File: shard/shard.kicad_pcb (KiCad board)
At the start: 2 copper layers, 35 x 25 mm, 2 parts, among them J0 Shard

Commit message: shard template fixed
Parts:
- J0: moved to F.Cu
- moved J0 2.50 mm to (125.0, 57.5), turned to 90 degrees
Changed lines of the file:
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@@
     )
   )
-  (module Connector_PinHeader_2.54mm:PinHeader_2x10_P2.54mm_Vertical (layer B.Cu)
-    (at 125 55 270)
+  (module Connector_PinHeader_2.54mm:PinHeader_2x10_P2.54mm_Vertical (layer F.Cu)
+    (at 125 57.5 90)
     (descr "Through hole straight pin header, 2x10, 2.54mm pitch, double rows")
     (tags "Through hole pin header THT 2x10 2.54mm double row")
-    (fp_text reference J0 (at 1.27 2.33 270) (layer B.Fab)
-      (effects (font (size 1 1) (thickness 0.15)) (justify mirror))
+    (fp_text reference J0 (at 1.27 -2.33 90) (layer F.Fab)
+      (effects (font (size 1 1) (thickness 0.15)))
     )
-    (fp_text value Shard (at 1.27 -25.19 270) (layer B.SilkS)
-      (effects (font (size 1 1) (thickness 0.15)) (justify mirror))
+    (fp_text value Shard (at 1.27 25.19 90) (layer F.SilkS)
+      (effects (font (size 1 1) (thickness 0.15)))
     )
-    (fp_line (start 0 1.27) (end 3.81 1.27) (layer B.Fab) (width 0.1))
-    (fp_line (start 3.81 1.27) (end 3.81 -24.13) (layer B.Fab) (width 0.1))
-    (fp_line (start 3.81 -24.13) (end -1.27 -24.13) (layer B.Fab) (width 0.1))
-    (fp_line (start -1.27 -24.13) (end -1.27 0) (layer B.Fab) (width 0.1))
-    (fp_line (start -1.27 0) (end 0 1.27) (layer B.Fab) (width 0.1))
-    (fp_line (start -1.33 -24.19) (end 3.87 -24.19) (layer B.SilkS) (width 0.12))
-    (fp_line (start -1.33 -1.27) (end -1.33 -24.19) (layer B.SilkS) (width 0.12))
-    (fp_line (start 3.87 1.33) (end 3.87 -24.19) (layer B.SilkS) (width 0.12))
-    (fp_line (start -1.33 -1.27) (end 1.27 -1.27) (layer B.SilkS) (width 0.12))
-    (fp_line (start 1.27 -1.27) (end 1.27 1.33) (layer B.SilkS) (width 0.12))
-    (fp_line (start 1.27 1.33) (end 3.87 1.33) (layer B.SilkS) (width 0.12))
-    (fp_line (start -1.33 0) (end -1.33 1.33) (layer B.SilkS) (width 0.12))
-    (fp_line (start -1.33 1.33) (end 0 1.33) (layer B.SilkS) (width 0.12))
-    (fp_line (start -1.8 1.8) (end -1.8 -24.65) (layer B.CrtYd) (width 0.05))
-    (fp_line (start -1.8 -24.65) (end 4.35 -24.65) (layer B.CrtYd) (width 0.05))
-    (fp_line (start 4.35 -24.65) (end 4.35 1.8) (layer B.CrtYd) (width 0.05))
-    (fp_line (start 4.35 1.8) (end -1.8 1.8) (layer B.CrtYd) (width 0.05))
-    (fp_text user %R (at 1.27 -11.43 180) (layer B.Fab)
-      (effects (font (size 1 1) (thickness 0.15)) (justify mirror))
+    (fp_line (start 0 -1.27) (end 3.81 -1.27) (layer F.Fab) (width 0.1))
+    (fp_line (start 3.81 -1.27) (end 3.81 24.13) (layer F.Fab) (width 0.1))
+    (fp_line (start 3.81 24.13) (end -1.27 24.13) (layer F.Fab) (width 0.1))
+    (fp_line (start -1.27 24.13) (end -1.27 0) (layer F.Fab) (width 0.1))
+    (fp_line (start -1.27 0) (end 0 -1.27) (layer F.Fab) (width 0.1))
+    (fp_line (start -1.33 24.19) (end 3.87 24.19) (layer F.SilkS) (width 0.12))
+    (fp_line (start -1.33 1.27) (end -1.33 24.19) (layer F.SilkS) (width 0.12))
+    (fp_line (start 3.87 -1.33) (end 3.87 24.19) (layer F.SilkS) (width 0.12))
+    (fp_line (start -1.33 1.27) (end 1.27 1.27) (layer F.SilkS) (width 0.12))
+    (fp_line (start 1.27 1.27) (end 1.27 -1.33) (layer F.SilkS) (width 0.12))
+    (fp_line (start 1.27 -1.33) (end 3.87 -1.33) (layer F.SilkS) (width 0.12))
+    (fp_line (start -1.33 0) (end -1.33 -1.33) (layer F.SilkS) (width 0.12))
+    (fp_line (start -1.33 -1.33) (end 0 -1.33) (layer F.SilkS) (width 0.12))
+    (fp_line (start -1.8 -1.8) (end -1.8 24.65) (layer F.CrtYd) (width 0.05))
+    (fp_line (start -1.8 24.65) (end 4.35 24.65) (layer F.CrtYd) (width 0.05))
+    (fp_line (start 4.35 24.65) (end 4.35 -1.8) (layer F.CrtYd) (width 0.05))
+    (fp_line (start 4.35 -1.8) (end -1.8 -1.8) (layer F.CrtYd) (width 0.05))
+    (fp_text user %R (at 1.27 11.43 180) (layer F.Fab)
+      (effects (font (size 1 1) (thickness 0.15)))
     )
-    (pad 1 thru_hole rect (at 0 0 270) (size 1.7 1.7) (drill 1) (layers *.Cu *.Mask)
+    (pad 1 thru_hole rect (at 0 0 90) (size 1.7 1.7) (drill 1) (layers *.Cu *.Mask)
       (net 1 +3V3))
-    (pad 2 thru_hole oval (at 2.54 0 270) (size 1.7 1.7) (drill 1) (layers *.Cu *.Mask)
+    (pad 2 thru_hole oval (at 2.54 0 90) (size 1.7 1.7) (drill 1) (layers *.Cu *.Mask)
       (net 3 D_CS))
-    (pad 3 thru_hole oval (at 0 -2.54 270) (size 1.7 1.7) (drill 1) (layers *.Cu *.Mask)
+    (pad 3 thru_hole oval (at 0 2.54 90) (size 1.7 1.7) (drill 1) (layers *.Cu *.Mask)
       (net 4 UP))
-    (pad 4 thru_hole oval (at 2.54 -2.54 270) (size 1.7 1.7) (drill 1) (layers *.Cu *.Mask)
+    (pad 4 thru_hole oval (at 2.54 2.54 90) (size 1.7 1.7) (drill 1) (layers *.Cu *.Mask)
       (net 5 D_DC))
-    (pad 5 thru_hole oval (at 0 -5.08 270) (size 1.7 1.7) (drill 1) (layers *.Cu *.Mask)
+    (pad 5 thru_hole oval (at 0 5.08 90) (size 1.7 1.7) (drill 1) (layers *.Cu *.Mask)
       (net 6 DOWN))
-    (pad 6 thru_hole oval (at 2.54 -5.08 270) (size 1.7 1.7) (drill 1) (layers *.Cu *.Mask)
+    (pad 6 thru_hole oval (at 2.54 5.08 90) (size 1.7 1.7) (drill 1) (layers *.Cu *.Mask)
       (net 7 D_RST))
-    (pad 7 thru_hole oval (at 0 -7.62 270) (size 1.7 1.7) (drill 1) (layers *.Cu *.Mask)
+    (pad 7 thru_hole oval (at 0 7.62 90) (size 1.7 1.7) (drill 1) (layers *.Cu *.Mask)
       (net 8 LEFT))
-    (pad 8 thru_hole oval (at 2.54 -7.62 270) (size 1.7 1.7) (drill 1) (layers *.Cu *.Mask)
+    (pad 8 thru_hole oval (at 2.54 7.62 90) (size 1.7 1.7) (drill 1) (layers *.Cu *.Mask)
       (net 9 D_MOSI))
-    (pad 9 thru_hole oval (at 0 -10.16 270) (size 1.7 1.7) (drill 1) (layers *.Cu *.Mask)
+    (pad 9 thru_hole oval (at 0 10.16 90) (size 1.7 1.7) (drill 1) (layers *.Cu *.Mask)
       (net 10 RIGHT))
-    (pad 10 thru_hole oval (at 2.54 -10.16 270) (size 1.7 1.7) (drill 1) (layers *.Cu *.Mask)
+    (pad 10 thru_hole oval (at 2.54 10.16 90) (size 1.7 1.7) (drill 1) (layers *.Cu *.Mask)
       (net 11 D_SCK))
-    (pad 11 thru_hole oval (at 0 -12.7 270) (size 1.7 1.7) (drill 1) (layers *.Cu *.Mask)
+    (pad 11 thru_hole oval (at 0 12.7 90) (size 1.7 1.7) (drill 1) (layers *.Cu *.Mask)
       (net 12 SND))
-    (pad 12 thru_hole oval (at 2.54 -12.7 270) (size 1.7 1.7) (drill 1) (layers *.Cu *.Mask)
+    (pad 12 thru_hole oval (at 2.54 12.7 90) (size 1.7 1.7) (drill 1) (layers *.Cu *.Mask)
       (net 2 D+))
-    (pad 13 thru_hole oval (at 0 -15.24 270) (size 1.7 1.7) (drill 1) (layers *.Cu *.Mask)
+    (pad 13 thru_hole oval (at 0 15.24 90) (size 1.7 1.7) (drill 1) (layers *.Cu *.Mask)
       (net 13 RESET))
-    (pad 14 thru_hole oval (at 2.54 -15.24 270) (size 1.7 1.7) (drill 1) (layers *.Cu *.Mask)
+    (pad 14 thru_hole oval (at 2.54 15.24 90) (size 1.7 1.7) (drill 1) (layers *.Cu *.Mask)
       (net 2 D+))
-    (pad 15 thru_hole oval (at 0 -17.78 270) (size 1.7 1.7) (drill 1) (layers *.Cu *.Mask)
+    (pad 15 thru_hole oval (at 0 17.78 90) (size 1.7 1.7) (drill 1) (layers *.Cu *.Mask)
       (net 14 BTN_C))
-    (pad 16 thru_hole oval (at 2.54 -17.78 270) (size 1.7 1.7) (drill 1) (layers *.Cu *.Mask)
+    (pad 16 thru_hole oval (at 2.54 17.78 90) (size 1.7 1.7) (drill 1) (layers *.Cu *.Mask)
       (net 2 D+))
-    (pad 17 thru_hole oval (at 0 -20.32 270) (size 1.7 1.7) (drill 1) (layers *.Cu *.Mask)
+    (pad 17 thru_hole oval (at 0 20.32 90) (size 1.7 1.7) (drill 1) (layers *.Cu *.Mask)
       (net 15 BTN_B))
-    (pad 18 thru_hole oval (at 2.54 -20.32 270) (size 1.7 1.7) (drill 1) (layers *.Cu *.Mask)
+    (pad 18 thru_hole oval (at 2.54 20.32 90) (size 1.7 1.7) (drill 1) (layers *.Cu *.Mask)
       (net 2 D+))
-    (pad 19 thru_hole oval (at 0 -22.86 270) (size 1.7 1.7) (drill 1) (layers *.Cu *.Mask)
+    (pad 19 thru_hole oval (at 0 22.86 90) (size 1.7 1.7) (drill 1) (layers *.Cu *.Mask)
       (net 16 BTN_A))
-    (pad 20 thru_hole oval (at 2.54 -22.86 270) (size 1.7 1.7) (drill 1) (layers *.Cu *.Mask)
+    (pad 20 thru_hole oval (at 2.54 22.86 90) (size 1.7 1.7) (drill 1) (layers *.Cu *.Mask)
       (net 2 D+))
     (model ${KISYS3DMOD}/Connector_PinHeader_2.54mm.3dshapes/PinHeader_2x10_P2.54mm_Vertical.wrl

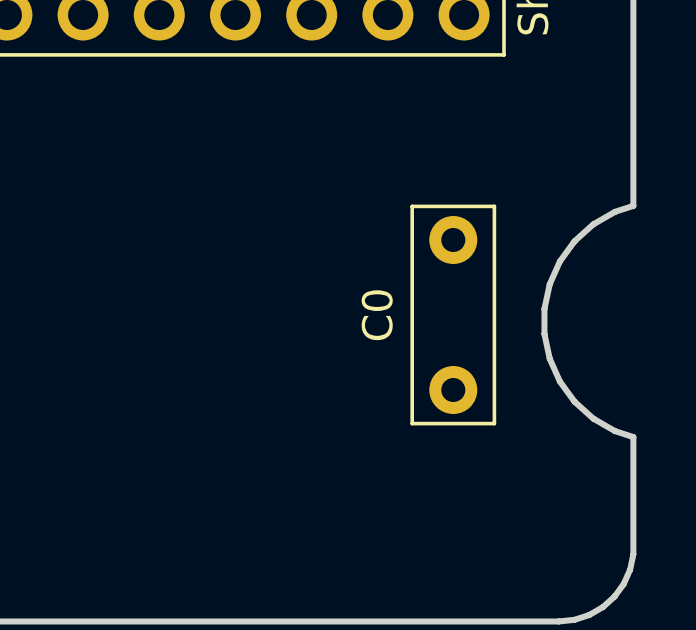
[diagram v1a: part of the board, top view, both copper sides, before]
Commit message: added capacitor value
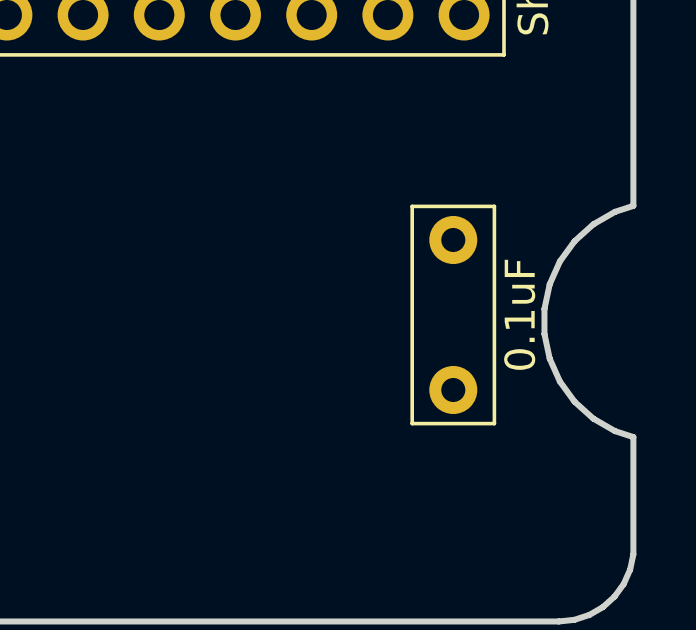
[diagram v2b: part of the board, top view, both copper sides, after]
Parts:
- C0: value C -> 0.1uF
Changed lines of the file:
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@@
     (descr "C, Rect series, Radial, pin pitch=5.00mm, , length*width=7*2.5mm^2, Capacitor")
     (tags "C Rect series Radial pin pitch 5.00mm  length 7mm width 2.5mm Capacitor")
-    (fp_text reference C0 (at 2.5 -2.5 90) (layer F.SilkS)
+    (fp_text reference C0 (at 2.5 0 90) (layer F.Fab)
       (effects (font (size 1 1) (thickness 0.15)))
     )
-    (fp_text value C (at 2.5 2.5 90) (layer F.Fab)
+    (fp_text value 0.1uF (at 2.5 2.25 90) (layer F.SilkS)
       (effects (font (size 1 1) (thickness 0.15)))
     )

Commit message: disconnected D- & D+ to fix GND net
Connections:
- net D+ renamed GND
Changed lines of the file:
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@@
   (net 0 "")
   (net 1 +3V3)
-  (net 2 D+)
-  (net 3 D_CS)
-  (net 4 UP)
-  (net 5 D_DC)
-  (net 6 DOWN)
-  (net 7 D_RST)
-  (net 8 LEFT)
-  (net 9 D_MOSI)
-  (net 10 RIGHT)
-  (net 11 D_SCK)
-  (net 12 SND)
-  (net 13 RESET)
-  (net 14 BTN_C)
-  (net 15 BTN_B)
-  (net 16 BTN_A)
+  (net 2 D_CS)
+  (net 3 UP)
+  (net 4 D_DC)
+  (net 5 DOWN)
+  (net 6 D_RST)
+  (net 7 LEFT)
+  (net 8 D_MOSI)
+  (net 9 RIGHT)
+  (net 10 D_SCK)
+  (net 11 SND)
+  (net 12 RESET)
+  (net 13 BTN_C)
+  (net 14 BTN_B)
+  (net 15 BTN_A)
+  (net 16 GND)
   (net_class Default "This is the default net class."
     (clearance 0.2)
@@
     (add_net BTN_B)
     (add_net BTN_C)
-    (add_net D+)
     (add_net DOWN)
     (add_net D_CS)
@@
     (add_net D_RST)
     (add_net D_SCK)
+    (add_net GND)
     (add_net LEFT)
     (add_net RESET)
@@
       (net 1 +3V3))
     (pad 2 thru_hole circle (at 5 0 90) (size 1.6 1.6) (drill 0.8) (layers *.Cu *.Mask)
-      (net 2 D+))
+      (net 16 GND))
     (model ${KISYS3DMOD}/Capacitor_THT.3dshapes/C_Rect_L7.0mm_W2.5mm_P5.00mm.wrl
       (at (xyz 0 0 0))
@@
       (net 1 +3V3))
     (pad 2 thru_hole oval (at 2.54 0 90) (size 1.7 1.7) (drill 1) (layers *.Cu *.Mask)
-      (net 3 D_CS))
+      (net 2 D_CS))
     (pad 3 thru_hole oval (at 0 2.54 90) (size 1.7 1.7) (drill 1) (layers *.Cu *.Mask)
-      (net 4 UP))
+      (net 3 UP))
     (pad 4 thru_hole oval (at 2.54 2.54 90) (size 1.7 1.7) (drill 1) (layers *.Cu *.Mask)
-      (net 5 D_DC))
+      (net 4 D_DC))
     (pad 5 thru_hole oval (at 0 5.08 90) (size 1.7 1.7) (drill 1) (layers *.Cu *.Mask)
-      (net 6 DOWN))
+      (net 5 DOWN))
     (pad 6 thru_hole oval (at 2.54 5.08 90) (size 1.7 1.7) (drill 1) (layers *.Cu *.Mask)
-      (net 7 D_RST))
+      (net 6 D_RST))
     (pad 7 thru_hole oval (at 0 7.62 90) (size 1.7 1.7) (drill 1) (layers *.Cu *.Mask)
-      (net 8 LEFT))
+      (net 7 LEFT))
     (pad 8 thru_hole oval (at 2.54 7.62 90) (size 1.7 1.7) (drill 1) (layers *.Cu *.Mask)
-      (net 9 D_MOSI))
+      (net 8 D_MOSI))
     (pad 9 thru_hole oval (at 0 10.16 90) (size 1.7 1.7) (drill 1) (layers *.Cu *.Mask)
-      (net 10 RIGHT))
+      (net 9 RIGHT))
     (pad 10 thru_hole oval (at 2.54 10.16 90) (size 1.7 1.7) (drill 1) (layers *.Cu *.Mask)
-      (net 11 D_SCK))
+      (net 10 D_SCK))
     (pad 11 thru_hole oval (at 0 12.7 90) (size 1.7 1.7) (drill 1) (layers *.Cu *.Mask)
-      (net 12 SND))
+      (net 11 SND))
     (pad 12 thru_hole oval (at 2.54 12.7 90) (size 1.7 1.7) (drill 1) (layers *.Cu *.Mask)
-      (net 2 D+))
+      (net 16 GND))
     (pad 13 thru_hole oval (at 0 15.24 90) (size 1.7 1.7) (drill 1) (layers *.Cu *.Mask)
-      (net 13 RESET))
+      (net 12 RESET))
     (pad 14 thru_hole oval (at 2.54 15.24 90) (size 1.7 1.7) (drill 1) (layers *.Cu *.Mask)
-      (net 2 D+))
+      (net 16 GND))
     (pad 15 thru_hole oval (at 0 17.78 90) (size 1.7 1.7) (drill 1) (layers *.Cu *.Mask)
-      (net 14 BTN_C))
+      (net 13 BTN_C))
     (pad 16 thru_hole oval (at 2.54 17.78 90) (size 1.7 1.7) (drill 1) (layers *.Cu *.Mask)
-      (net 2 D+))
+      (net 16 GND))
     (pad 17 thru_hole oval (at 0 20.32 90) (size 1.7 1.7) (drill 1) (layers *.Cu *.Mask)
-      (net 15 BTN_B))
+      (net 14 BTN_B))
     (pad 18 thru_hole oval (at 2.54 20.32 90) (size 1.7 1.7) (drill 1) (layers *.Cu *.Mask)
-      (net 2 D+))
+      (net 16 GND))
     (pad 19 thru_hole oval (at 0 22.86 90) (size 1.7 1.7) (drill 1) (layers *.Cu *.Mask)
-      (net 16 BTN_A))
+      (net 15 BTN_A))
     (pad 20 thru_hole oval (at 2.54 22.86 90) (size 1.7 1.7) (drill 1) (layers *.Cu *.Mask)
-      (net 2 D+))
+      (net 16 GND))
     (model ${KISYS3DMOD}/Connector_PinHeader_2.54mm.3dshapes/PinHeader_2x10_P2.54mm_Vertical.wrl
       (at (xyz 0 0 0))

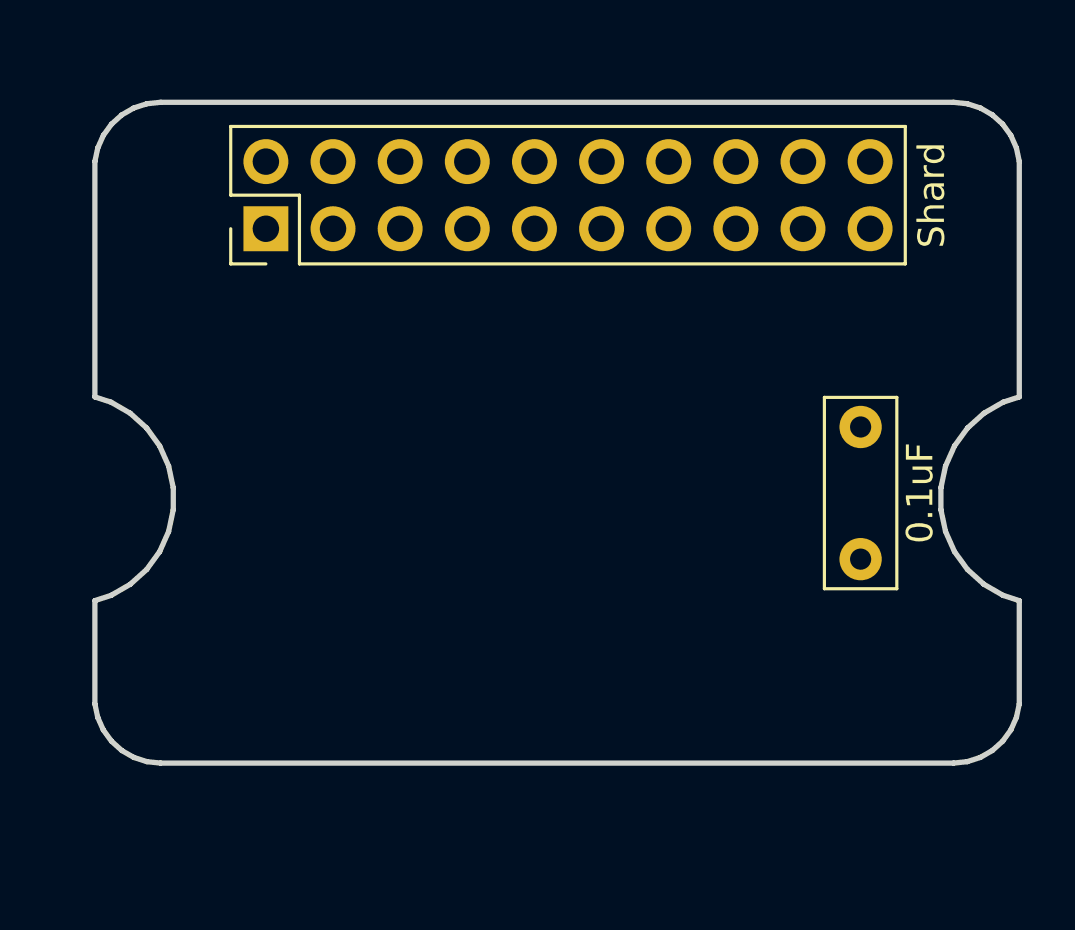
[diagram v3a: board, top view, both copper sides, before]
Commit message: Template updated to edge connector
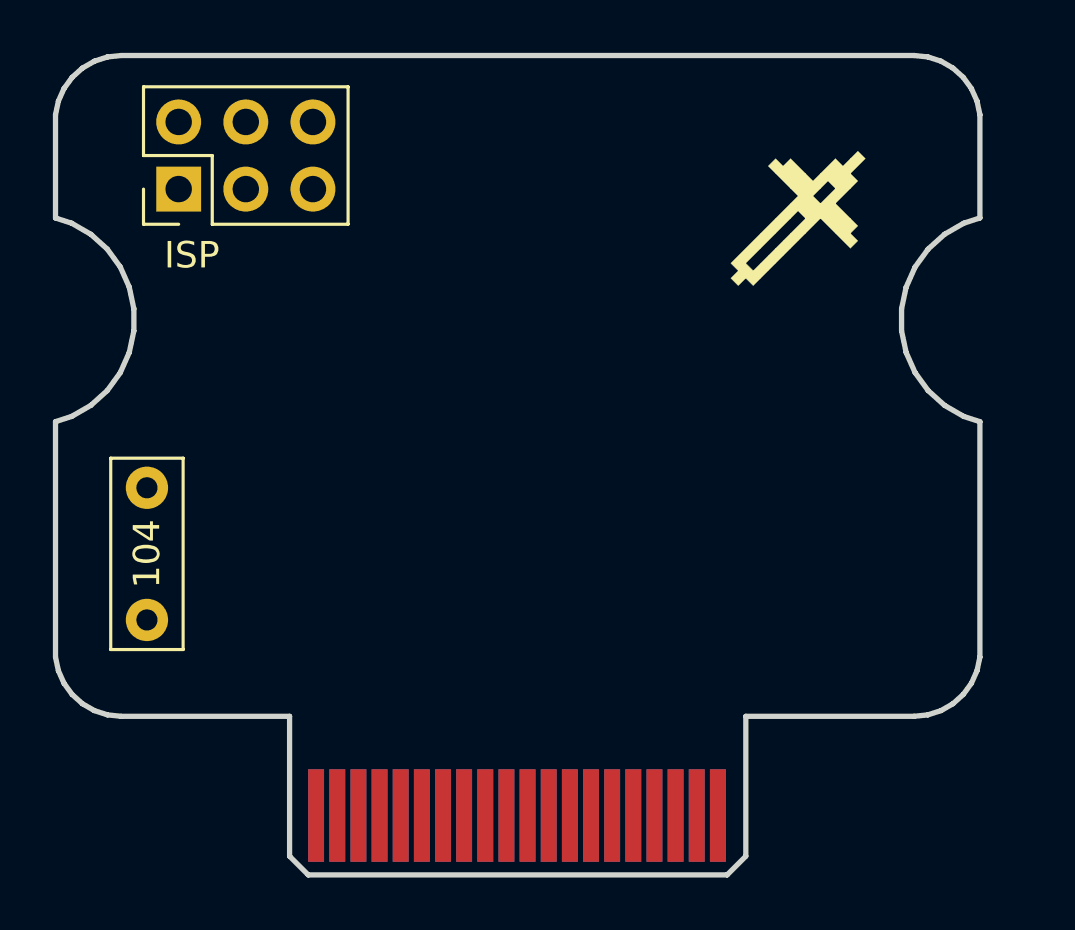
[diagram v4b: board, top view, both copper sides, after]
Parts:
- added J1: ISP, Connector_PinHeader_2.54mm:PinHeader_2x03_P2.54mm_Vertical, F.Cu at (121.7, 56.0)
- added SPIKE: , SPIKE, F.Cu at (145.7, 52.3)
- C0: value 0.1uF -> 104
- J0: footprint Connector_PinHeader_2.54mm:PinHeader_2x10_P2.54mm_Vertical -> Custom Footprints:Samtec_MEC8-120-02-L-D-RA1_Edge
- moved C0 27.1 mm to (120.5, 72.3)
- moved J0 23.9 mm to (126.9, 81.3), turned to 0 degrees
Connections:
- J0 pad 1: +3V3 -> Net-(J0-Pad1)
- J0 pad 10: D_SCK -> BTN_B
- J0 pad 11: SND -> Net-(J0-Pad11)
- J0 pad 12: GND -> BTN_C
- J0 pad 13: RESET -> Net-(J0-Pad13)
- J0 pad 14: GND -> Net-(J0-Pad14)
- J0 pad 15: BTN_C -> Net-(J0-Pad15)
- J0 pad 16: GND -> RESET
- J0 pad 17: BTN_B -> Net-(J0-Pad17)
- J0 pad 18: GND -> Net-(J0-Pad18)
- J0 pad 19: BTN_A -> Net-(J0-Pad19)
- J0 pad 2: D_CS -> +3V3
- J0 pad 20: GND -> D_DC
- J0 pad 3: UP -> Net-(J0-Pad3)
- J0 pad 4: D_DC -> D-
- J0 pad 5: DOWN -> Net-(J0-Pad5)
- J0 pad 6: D_RST -> D+
- J0 pad 7: LEFT -> Net-(J0-Pad7)
- J0 pad 8: D_MOSI -> BTN_A
- J0 pad 9: RIGHT -> Net-(J0-Pad9)
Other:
- board size 35 x 25 mm -> 35 x 31 mm

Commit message: ::eyeroll::
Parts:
- moved J1 6.26 mm to (127.3, 53.2), turned to 270 degrees
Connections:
- J0 pad 1: Net-(J0-Pad1) -> (no net)
- J0 pad 10: BTN_B -> (no net)
- J0 pad 11: Net-(J0-Pad11) -> (no net)
- J0 pad 12: BTN_C -> (no net)
- J0 pad 13: Net-(J0-Pad13) -> (no net)
- J0 pad 14: Net-(J0-Pad14) -> (no net)
- J0 pad 15: Net-(J0-Pad15) -> (no net)
- J0 pad 17: Net-(J0-Pad17) -> (no net)
- J0 pad 18: Net-(J0-Pad18) -> (no net)
- J0 pad 19: Net-(J0-Pad19) -> (no net)
- J0 pad 20: D_DC -> (no net)
- J0 pad 21: Net-(J0-Pad21) -> (no net)
- J0 pad 22: D_CS -> (no net)
- J0 pad 23: Net-(J0-Pad23) -> (no net)
- J0 pad 24: D_RST -> (no net)
- J0 pad 25: Net-(J0-Pad25) -> (no net)
- J0 pad 26: D_MOSI -> (no net)
- J0 pad 27: Net-(J0-Pad27) -> (no net)
- J0 pad 28: D_SCK -> (no net)
- J0 pad 29: Net-(J0-Pad29) -> (no net)
- J0 pad 3: Net-(J0-Pad3) -> (no net)
- J0 pad 30: SND -> (no net)
- J0 pad 31: Net-(J0-Pad31) -> (no net)
- J0 pad 32: UP -> (no net)
- J0 pad 33: Net-(J0-Pad33) -> (no net)
- J0 pad 34: DOWN -> (no net)
- J0 pad 35: Net-(J0-Pad35) -> (no net)
- J0 pad 36: LEFT -> (no net)
- J0 pad 37: Net-(J0-Pad37) -> (no net)
- J0 pad 38: RIGHT -> (no net)
- J0 pad 39: Net-(J0-Pad39) -> (no net)
- J0 pad 4: D- -> (no net)
- J0 pad 5: Net-(J0-Pad5) -> (no net)
- J0 pad 6: D+ -> (no net)
- J0 pad 7: Net-(J0-Pad7) -> (no net)
- J0 pad 8: BTN_A -> (no net)
- J0 pad 9: Net-(J0-Pad9) -> (no net)
- J1 pad 1: MISO -> (no net)
- J1 pad 3: SCK -> (no net)
- J1 pad 4: MOSI -> (no net)
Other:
- board text added: "."
